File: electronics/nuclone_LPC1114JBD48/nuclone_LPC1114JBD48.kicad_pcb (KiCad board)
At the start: 2 copper layers, 48.3 x 76.2 mm, 29 parts, among them J1 JTAG_2X05, J2 USB-ID, J3 nuclone_small_left, J4 nuclone_small_right, SW1 RESET, U1 MCP1702-MB

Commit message: initial import of components
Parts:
- added C3: 12p, SquantorRcl:C_0402, F.Cu at (74.5, 88.0)
- added C4: 12p, SquantorRcl:C_0402, F.Cu at (74.5, 93.2)
- added C5: 1u, SquantorRcl:C_0402, F.Cu at (84.4, 83.9)
- added C6: 1u, SquantorRcl:C_0402, F.Cu at (77.6, 93.3)
- added C7: 100n, SquantorRcl:C_0402, F.Cu at (77.6, 92.2)
- added C8: 100n, SquantorRcl:C_0402, F.Cu at (85.5, 83.9)
- added JP1: reset, SquantorSpecial:solder_jumper_2way_noconn, B.Cu at (80.7, 89.7)
- added JP2: reset, SquantorSpecial:solder_jumper_2way_noconn, B.Cu at (89.5, 92.2)
- added JP3: SWDIO, SquantorSpecial:solder_jumper_2way_noconn, B.Cu at (86.8, 87.1)
- added U2: LPC1114FBD48_302, SquantorIC:SOT313-2-NXP, F.Cu at (85.1, 91.4)
- added Y1: 12MHz, SquantorCrystal:Crystal_3225_4, F.Cu at (74.5, 90.6)
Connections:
- J3 pad 10: /GPIO_03 -> /PIO0_1
- J3 pad 11: /GPIO_04 -> /PIO1_8
- J3 pad 12: /GPIO_05 -> /PIO0_2
- J3 pad 13: /GPIO_06 -> /PIO2_7
- J3 pad 14: /GPIO_07 -> /PIO2_8
- J3 pad 15: /GPIO_08 -> /PIO2_1
- J3 pad 16: /GPIO_09 -> /PIO0_3
- J3 pad 17: /GPIO_10 -> /PIO0_4
- J3 pad 18: /GPIO_11 -> /PIO0_5
- J3 pad 19: /GPIO_12 -> /PIO1_9
- J3 pad 20: /GPIO_13 -> /PIO3_4
- J3 pad 23: /GPIO_14 -> /PIO2_4
- J3 pad 24: /GPIO_15 -> /PIO2_5
- J3 pad 25: /GPIO_16 -> /PIO3_5
- J3 pad 26: /GPIO_17 -> /PIO0_6
- J3 pad 27: /GPIO_18 -> /PIO0_7
- J3 pad 28: /GPIO_19 -> /PIO2_9
- J3 pad 7: /GPIO_00 -> /PIO2_6
- J3 pad 8: /GPIO_01 -> /PIO2_0
- J3 pad 9: /GPIO_02 -> /PIO0_0
- J4 pad 13: /GPIO_40 -> /PIO2_10
- J4 pad 14: /GPIO_41 -> /PIO2_2
- J4 pad 15: /GPIO_42 -> /PIO0_8
- J4 pad 16: /GPIO_43 -> /PIO0_9
- J4 pad 17: /GPIO_44 -> /PIO0_10
- J4 pad 18: /GPIO_45 -> /PIO1_10
- J4 pad 21: /GPIO_46 -> /PIO2_11
- J4 pad 22: /GPIO_47 -> /PIO0_11
- J4 pad 23: /GPIO_48 -> /PIO1_0
- J4 pad 24: /GPIO_49 -> /PIO1_1
- J4 pad 25: /GPIO_50 -> /PIO1_2
- J4 pad 26: /GPIO_51 -> /PIO3_0
- J4 pad 27: /GPIO_52 -> /PIO3_1
- J4 pad 28: /GPIO_53 -> /PIO2_3
- J4 pad 29: /GPIO_54 -> /PIO1_3
- J4 pad 30: /GPIO_55 -> /PIO1_4
- J4 pad 31: /GPIO_56 -> /PIO1_11
- J4 pad 32: /GPIO_57 -> /PIO3_2
- J4 pad 33: /GPIO_58 -> /PIO1_5
- J4 pad 34: /GPIO_59 -> /PIO1_6
- J4 pad 35: /GPIO_60 -> /PIO1_7
- J4 pad 36: /GPIO_61 -> /PIO3_3

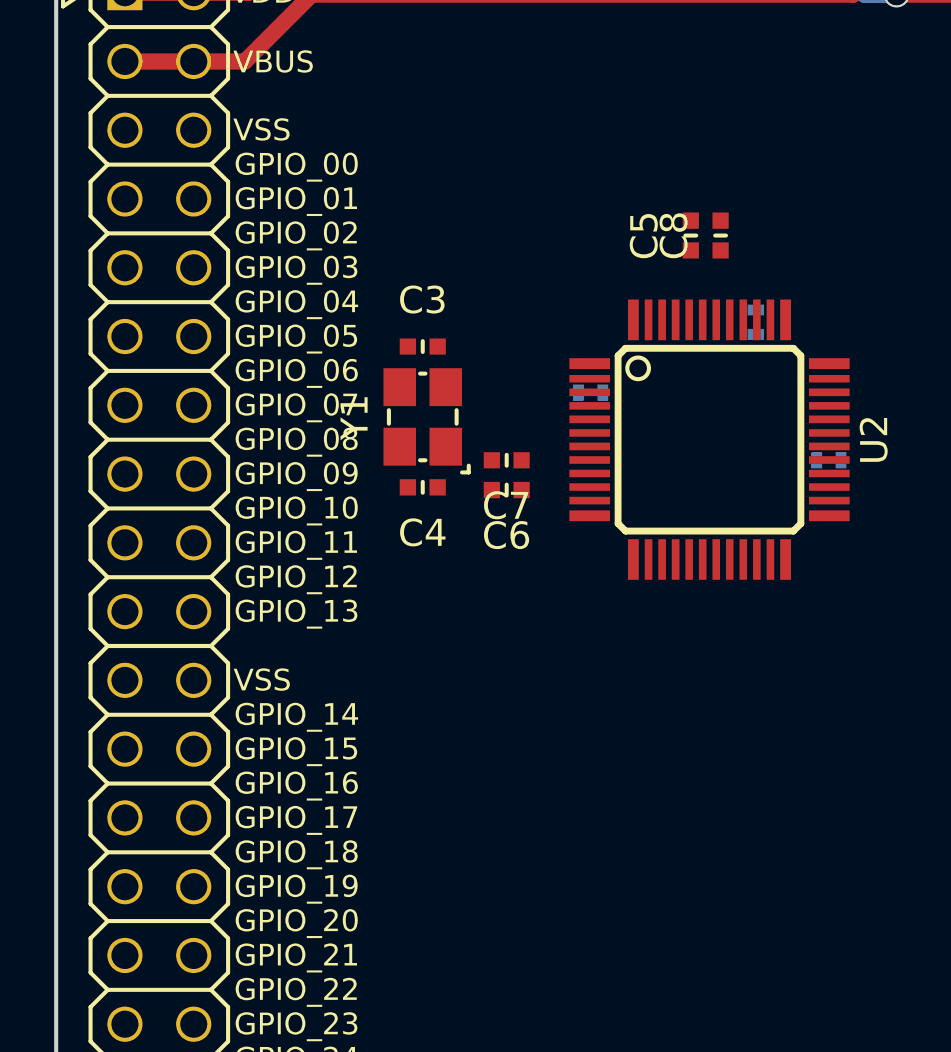
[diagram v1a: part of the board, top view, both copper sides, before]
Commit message: WIP routing traces left connector
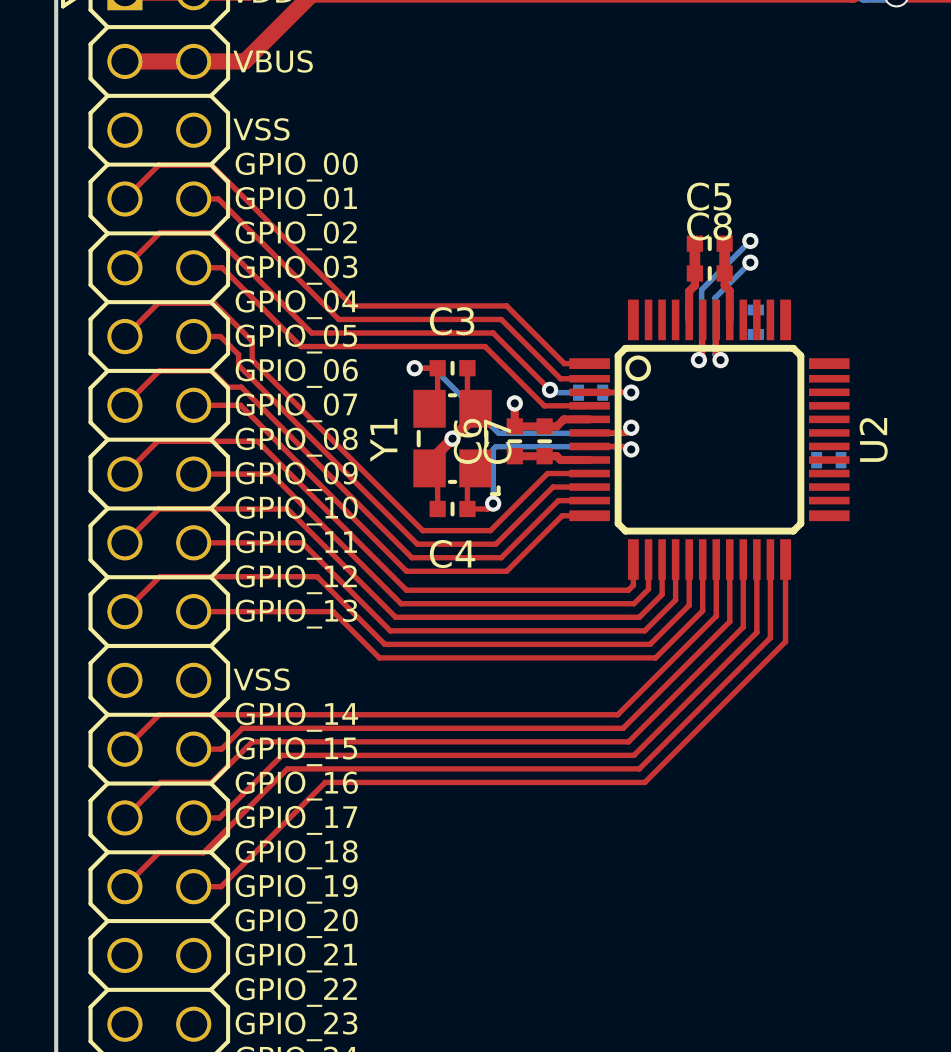
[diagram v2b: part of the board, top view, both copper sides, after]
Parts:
- moved C6 1.82 mm to (77.9, 91.5), turned to 90 degrees
- moved C7 1.57 mm to (79.0, 91.5), turned to 90 degrees
- moved C8 1.46 mm to (85.1, 85.3), turned to 0 degrees
- moved Y1 1.36 mm to (75.6, 91.4)
- moved C3 1.36 mm to (75.6, 88.8)
- moved C4 1.36 mm to (75.6, 94.0)
- moved C5 0.76 mm to (85.1, 84.2), turned to 0 degrees
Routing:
- net /PIO0_7: track 0.00 -> 30.5 mm
- net /PIO2_9: track 0.00 -> 28.6 mm
- net /PIO3_5: track 0.00 -> 28.3 mm
- net /PIO0_6: track 0.00 -> 26.3 mm
- net /PIO2_4: track 0.00 -> 26.0 mm
- net /PIO1_9: track 0.00 -> 24.7 mm
- net /PIO2_5: track 0.00 -> 24.0 mm
- net /PIO0_4: track 0.00 -> 23.7 mm
- net /PIO2_1: track 0.00 -> 22.6 mm
- net /PIO1_8: track 0.00 -> 22.4 mm
- net /PIO3_4: track 0.00 -> 22.1 mm
- net /PIO2_7: track 0.00 -> 21.4 mm
- net /PIO0_5: track 0.00 -> 21.1 mm
- net /PIO2_6: track 0.00 -> 20.7 mm
- net /PIO0_3: track 0.00 -> 20.1 mm
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
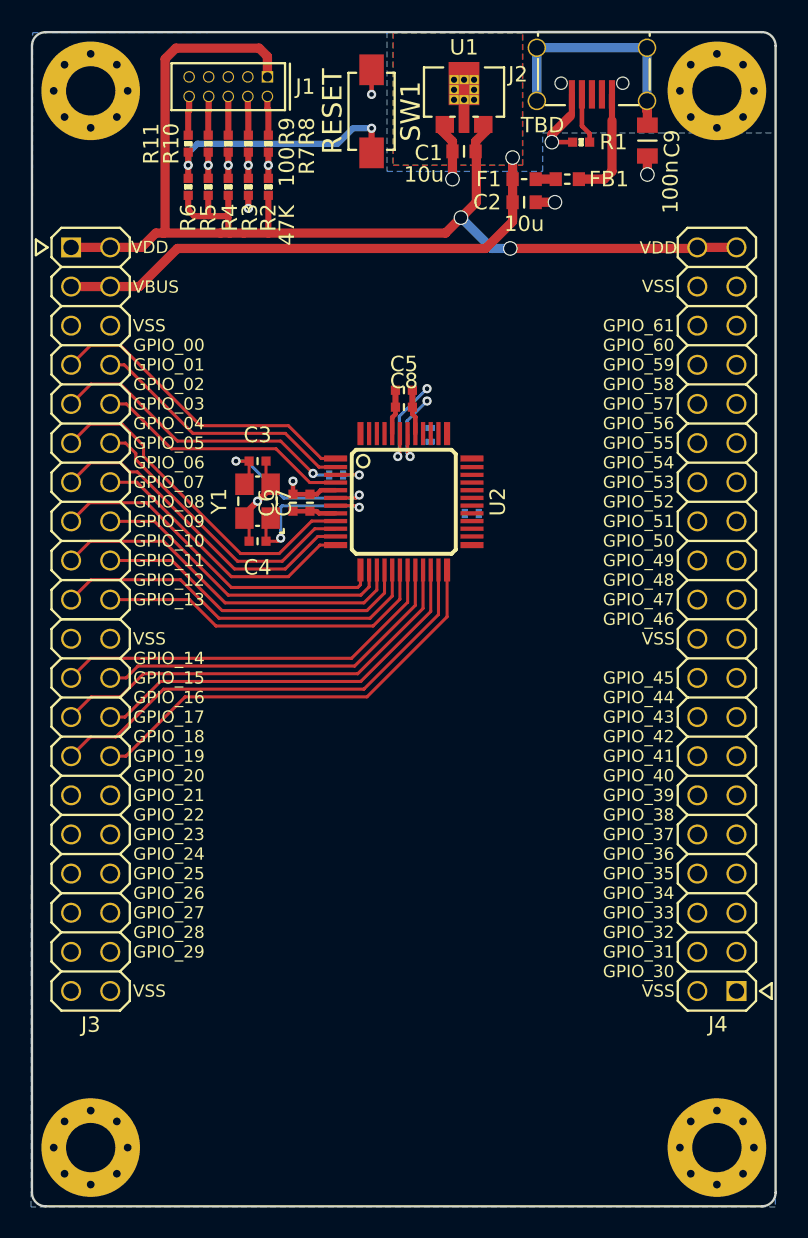
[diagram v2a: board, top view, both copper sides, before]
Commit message: right side connector routed
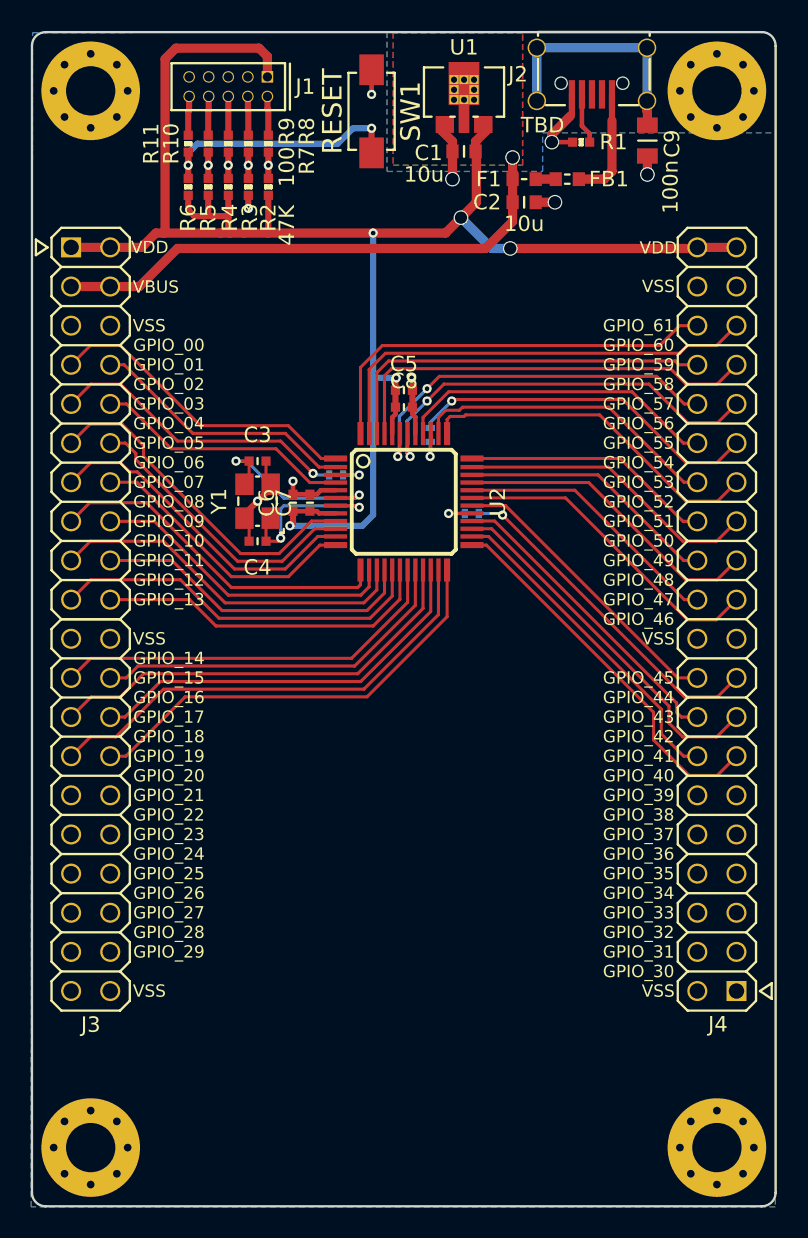
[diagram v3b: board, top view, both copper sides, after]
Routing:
- net /PIO1_7: track 0.00 -> 29.2 mm
- net /PIO1_5: track 0.00 -> 27.7 mm
- net /VDD: track 87.4 -> 114.8 mm, vias 2 -> 5
- net /PIO3_3: track 0.00 -> 27.3 mm
- net /PIO1_6: track 0.00 -> 25.2 mm
- net /PIO2_10: track 0.00 -> 24.9 mm
- net /PIO0_8: track 0.00 -> 23.9 mm
- net /PIO1_3: track 0.00 -> 23.1 mm, vias 0 -> 1
- net /PIO3_1: track 0.00 -> 22.6 mm
- net /PIO0_10: track 0.00 -> 22.2 mm, vias 0 -> 1
- net /PIO1_11: track 5.77 -> 27.8 mm
- net /PIO2_2: track 0.00 -> 21.5 mm
- net /PIO2_11: track 0.00 -> 21.0 mm
- net /PIO1_4: track 0.00 -> 20.9 mm
- net /PIO1_0: track 0.00 -> 20.3 mm
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
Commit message: all lines routed
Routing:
- net /TCK: track 4.27 -> 37.9 mm, vias 2 -> 4
- net /TMS: track 4.15 -> 32.8 mm, vias 2 -> 4
- net /RESET: track 19.2 -> 43.9 mm, vias 3 -> 4
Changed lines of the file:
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@@
     (thickness 1.6)
     (drawings 8)
-    (tracks 438)
+    (tracks 469)
     (zones 0)
     (modules 40)
@@
   )
   (setup
-    (last_trace_width 0.4)
+    (last_trace_width 0.2)
     (user_trace_width 0.15)
     (user_trace_width 0.2)
@@
   (segment (start 86.84 87.015) (end 86.84 88.46) (width 0.2) (layer F.Cu) (net 36))
   (segment (start 86.8 88.5) (end 86.8 87.55) (width 0.2) (layer B.Cu) (net 36))
+  (segment (start 86.8 87.55) (end 87.35 87.55) (width 0.2) (layer B.Cu) (net 36))
+  (segment (start 87.35 87.55) (end 87.6 87.3) (width 0.2) (layer B.Cu) (net 36))
+  (segment (start 87.6 87.3) (end 87.6 86.6) (width 0.2) (layer B.Cu) (net 36))
+  (segment (start 87.6 86.6) (end 88.9 85.3) (width 0.2) (layer B.Cu) (net 36))
+  (segment (start 88.9 85.3) (end 88.9 84.2) (width 0.2) (layer B.Cu) (net 36))
+  (via (at 88.3 80.6) (size 0.6) (drill 0.3) (layers F.Cu B.Cu) (net 36))
+  (segment (start 88.3 83.6) (end 88.3 80.6) (width 0.2) (layer B.Cu) (net 36))
+  (segment (start 88.9 84.2) (end 88.3 83.6) (width 0.2) (layer B.Cu) (net 36))
+  (segment (start 88.3 80.3) (end 88.3 80.6) (width 0.2) (layer F.Cu) (net 36))
+  (segment (start 88 80) (end 88.3 80.3) (width 0.2) (layer F.Cu) (net 36))
+  (segment (start 80.7 80) (end 88 80) (width 0.2) (layer F.Cu) (net 36))
+  (segment (start 76.7 76) (end 80.7 80) (width 0.2) (layer F.Cu) (net 36))
+  (via (at 76.7 76) (size 0.6) (drill 0.3) (layers F.Cu B.Cu) (net 36))
+  (segment (start 76.3 75.6) (end 76.3 69.6) (width 0.2) (layer B.Cu) (net 36))
+  (segment (start 76.7 76) (end 76.3 75.6) (width 0.2) (layer B.Cu) (net 36))
   (segment (start 75 68.75) (end 75 69.6) (width 0.4) (layer F.Cu) (net 37))
   (via (at 75 69.6) (size 0.6) (drill 0.3) (layers F.Cu B.Cu) (net 37))
@@
   (segment (start 89.515 92.19) (end 88.01 92.19) (width 0.2) (layer F.Cu) (net 37))
   (segment (start 88 92.2) (end 89.05 92.2) (width 0.2) (layer B.Cu) (net 37))
+  (segment (start 86.1 91.3) (end 87 92.2) (width 0.2) (layer B.Cu) (net 37))
+  (segment (start 86.1 86.2) (end 86.1 91.3) (width 0.2) (layer B.Cu) (net 37))
+  (segment (start 87.3 85) (end 86.1 86.2) (width 0.2) (layer B.Cu) (net 37))
+  (segment (start 87.3 80.6) (end 87.3 85) (width 0.2) (layer B.Cu) (net 37))
+  (segment (start 87 92.2) (end 88 92.2) (width 0.2) (layer B.Cu) (net 37))
+  (via (at 87.3 80.6) (size 0.6) (drill 0.3) (layers F.Cu B.Cu) (net 37))
+  (segment (start 80.4 80.6) (end 87.3 80.6) (width 0.2) (layer F.Cu) (net 37))
+  (segment (start 75.8 76) (end 80.4 80.6) (width 0.2) (layer F.Cu) (net 37))
+  (via (at 75.8 76) (size 0.6) (drill 0.3) (layers F.Cu B.Cu) (net 37))
+  (segment (start 75.8 70.4) (end 75 69.6) (width 0.2) (layer B.Cu) (net 37))
+  (segment (start 75.8 76) (end 75.8 70.4) (width 0.2) (layer B.Cu) (net 37))
   (via (at 73.7 69.6) (size 0.6) (drill 0.3) (layers F.Cu B.Cu) (net 38))
   (segment (start 73.7 68.75) (end 73.7 69.6) (width 0.4) (layer F.Cu) (net 38))
@@
   (segment (start 80.665 89.69) (end 82.19 89.69) (width 0.2) (layer F.Cu) (net 40))
   (segment (start 82.2 89.7) (end 81.15 89.7) (width 0.2) (layer B.Cu) (net 40))
+  (segment (start 82.2 89.7) (end 82.2 88.6) (width 0.2) (layer F.Cu) (net 40))
+  (via (at 71.1 75.9) (size 0.6) (drill 0.3) (layers F.Cu B.Cu) (net 40))
+  (segment (start 71.1 77.5) (end 71.1 75.9) (width 0.2) (layer F.Cu) (net 40))
+  (segment (start 82.2 88.6) (end 71.1 77.5) (width 0.2) (layer F.Cu) (net 40))
+  (segment (start 71.1 75.9) (end 71.1 69.6) (width 0.2) (layer B.Cu) (net 40))
   (segment (start 75.05 90) (end 74.75 90.3) (width 0.2) (layer F.Cu) (net 41))
   (segment (start 75.05 88.8) (end 75.05 90) (width 0.2) (layer F.Cu) (net 41))
@@
   (segment (start 80.665 91.19) (end 82.01 91.19) (width 0.2) (layer F.Cu) (net 41))
   (segment (start 74.2 88.8) (end 75.05 88.8) (width 0.2) (layer F.Cu) (net 41))
-  (segment (start 82 91.2) (end 82.2 91) (width 0.2) (layer B.Cu) (net 41))
-  (segment (start 77.3 91.2) (end 82 91.2) (width 0.2) (layer B.Cu) (net 41))
-  (segment (start 74.9 88.8) (end 77.3 91.2) (width 0.2) (layer B.Cu) (net 41))
-  (segment (start 74.2 88.8) (end 74.9 88.8) (width 0.2) (layer B.Cu) (net 41))
   (via (at 74.2 88.8) (size 0.6) (drill 0.3) (layers F.Cu B.Cu) (net 41))
+  (segment (start 77.6 91.2) (end 82 91.2) (width 0.2) (layer B.Cu) (net 41))
+  (segment (start 75.2 88.8) (end 77.6 91.2) (width 0.2) (layer B.Cu) (net 41))
+  (segment (start 82 91.2) (end 82.2 91) (width 0.2) (layer B.Cu) (net 41))
+  (segment (start 74.2 88.8) (end 75.2 88.8) (width 0.2) (layer B.Cu) (net 41))
   (segment (start 76.15 92.8) (end 76.45 92.5) (width 0.2) (layer F.Cu) (net 42))
   (segment (start 76.15 94) (end 76.15 92.8) (width 0.2) (layer F.Cu) (net 42))
@@
   (via (at 77.1 93.8) (size 0.6) (drill 0.3) (layers F.Cu B.Cu) (net 42))
   (segment (start 82.1 91.7) (end 82.2 91.8) (width 0.2) (layer B.Cu) (net 42))
-  (segment (start 77.3 91.7) (end 82.1 91.7) (width 0.2) (layer B.Cu) (net 42))
-  (segment (start 77.1 91.9) (end 77.3 91.7) (width 0.2) (layer B.Cu) (net 42))
-  (segment (start 77.1 93.8) (end 77.1 91.9) (width 0.2) (layer B.Cu) (net 42))
+  (segment (start 77.6 91.7) (end 82.1 91.7) (width 0.2) (layer B.Cu) (net 42))
+  (segment (start 77.1 92.2) (end 77.6 91.7) (width 0.2) (layer B.Cu) (net 42))
+  (segment (start 77.1 93.8) (end 77.1 92.2) (width 0.2) (layer B.Cu) (net 42))
   (segment (start 64.81 104.1) (end 63.5 105.41) (width 0.2) (layer F.Cu) (net 43))
   (segment (start 66.7 104.1) (end 64.81 104.1) (width 0.2) (layer F.Cu) (net 43))
@@
   (segment (start 84.84 88.36) (end 84.7 88.5) (width 0.2) (layer F.Cu) (net 73))
   (segment (start 84.84 87.015) (end 84.84 88.36) (width 0.2) (layer F.Cu) (net 73))
-  (segment (start 84.7 88.5) (end 84.8 88.4) (width 0.2) (layer B.Cu) (net 73))
-  (via (at 86.6 84.1) (size 0.6) (drill 0.3) (layers F.Cu B.Cu) (net 73))
-  (segment (start 84.8 85.9) (end 86.6 84.1) (width 0.2) (layer B.Cu) (net 73))
-  (segment (start 84.8 88.4) (end 84.8 85.9) (width 0.2) (layer B.Cu) (net 73))
-  (segment (start 103.29 85.09) (end 104.14 85.09) (width 0.2) (layer F.Cu) (net 73))
   (segment (start 101.5 83.3) (end 103.29 85.09) (width 0.2) (layer F.Cu) (net 73))
-  (segment (start 87.4 83.3) (end 101.5 83.3) (width 0.2) (layer F.Cu) (net 73))
-  (segment (start 86.6 84.1) (end 87.4 83.3) (width 0.2) (layer F.Cu) (net 73))
+  (segment (start 86.6 83.6) (end 86.9 83.3) (width 0.2) (layer F.Cu) (net 73))
+  (segment (start 103.29 85.09) (end 104.14 85.09) (width 0.2) (layer F.Cu) (net 73))
+  (segment (start 84.8 88.4) (end 84.7 88.5) (width 0.2) (layer B.Cu) (net 73))
+  (segment (start 84.8 85.4) (end 84.8 88.4) (width 0.2) (layer B.Cu) (net 73))
+  (segment (start 86.6 83.6) (end 84.8 85.4) (width 0.2) (layer B.Cu) (net 73))
+  (segment (start 86.9 83.3) (end 101.5 83.3) (width 0.2) (layer F.Cu) (net 73))
+  (via (at 86.6 83.6) (size 0.6) (drill 0.3) (layers F.Cu B.Cu) (net 73))
   (via (at 85.5 88.5) (size 0.6) (drill 0.3) (layers F.Cu B.Cu) (net 74))
   (segment (start 85.34 88.34) (end 85.5 88.5) (width 0.2) (layer F.Cu) (net 74))
   (segment (start 85.34 87.015) (end 85.34 88.34) (width 0.2) (layer F.Cu) (net 74))
-  (segment (start 85.5 88.5) (end 85.3 88.3) (width 0.2) (layer B.Cu) (net 74))
-  (via (at 86.6 84.9) (size 0.6) (drill 0.3) (layers F.Cu B.Cu) (net 74))
-  (segment (start 85.3 86.2) (end 86.6 84.9) (width 0.2) (layer B.Cu) (net 74))
-  (segment (start 85.3 88.3) (end 85.3 86.2) (width 0.2) (layer B.Cu) (net 74))
-  (segment (start 86.6 84.9) (end 87.7 83.8) (width 0.2) (layer F.Cu) (net 74))
-  (segment (start 87.7 83.8) (end 101 83.8) (width 0.2) (layer F.Cu) (net 74))
-  (segment (start 101 83.8) (end 103.5 86.3) (width 0.2) (layer F.Cu) (net 74))
   (segment (start 105.47 86.3) (end 106.68 85.09) (width 0.2) (layer F.Cu) (net 74))
   (segment (start 103.5 86.3) (end 105.47 86.3) (width 0.2) (layer F.Cu) (net 74))
+  (segment (start 101 83.8) (end 103.5 86.3) (width 0.2) (layer F.Cu) (net 74))
+  (segment (start 87.3 83.8) (end 101 83.8) (width 0.2) (layer F.Cu) (net 74))
+  (segment (start 86.6 84.5) (end 87.3 83.8) (width 0.2) (layer F.Cu) (net 74))
+  (segment (start 85.3 88.3) (end 85.5 88.5) (width 0.2) (layer B.Cu) (net 74))
+  (segment (start 85.3 85.8) (end 85.3 88.3) (width 0.2) (layer B.Cu) (net 74))
+  (segment (start 86.6 84.5) (end 85.3 85.8) (width 0.2) (layer B.Cu) (net 74))
+  (via (at 86.6 84.5) (size 0.6) (drill 0.3) (layers F.Cu B.Cu) (net 74))
   (segment (start 86.34 87.015) (end 86.34 85.96) (width 0.2) (layer F.Cu) (net 75))
   (segment (start 86.34 85.96) (end 88 84.3) (width 0.2) (layer F.Cu) (net 75))
